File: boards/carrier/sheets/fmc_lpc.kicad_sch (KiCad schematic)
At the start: 4 parts

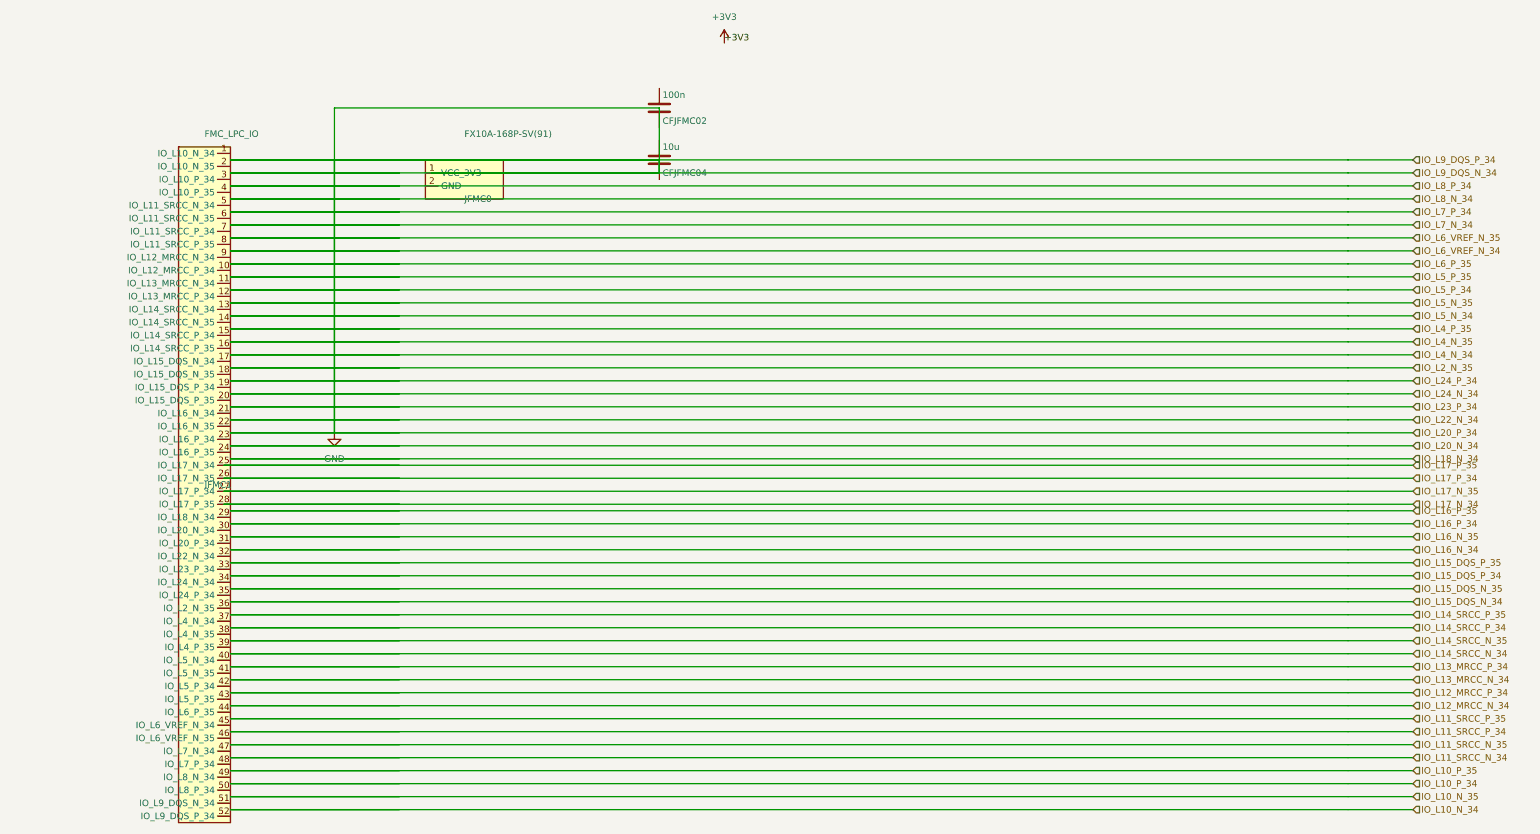
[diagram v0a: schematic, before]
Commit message: hdmi: use Connector_Generic:Conn_01x19 (Connector lib not auto-discovered)
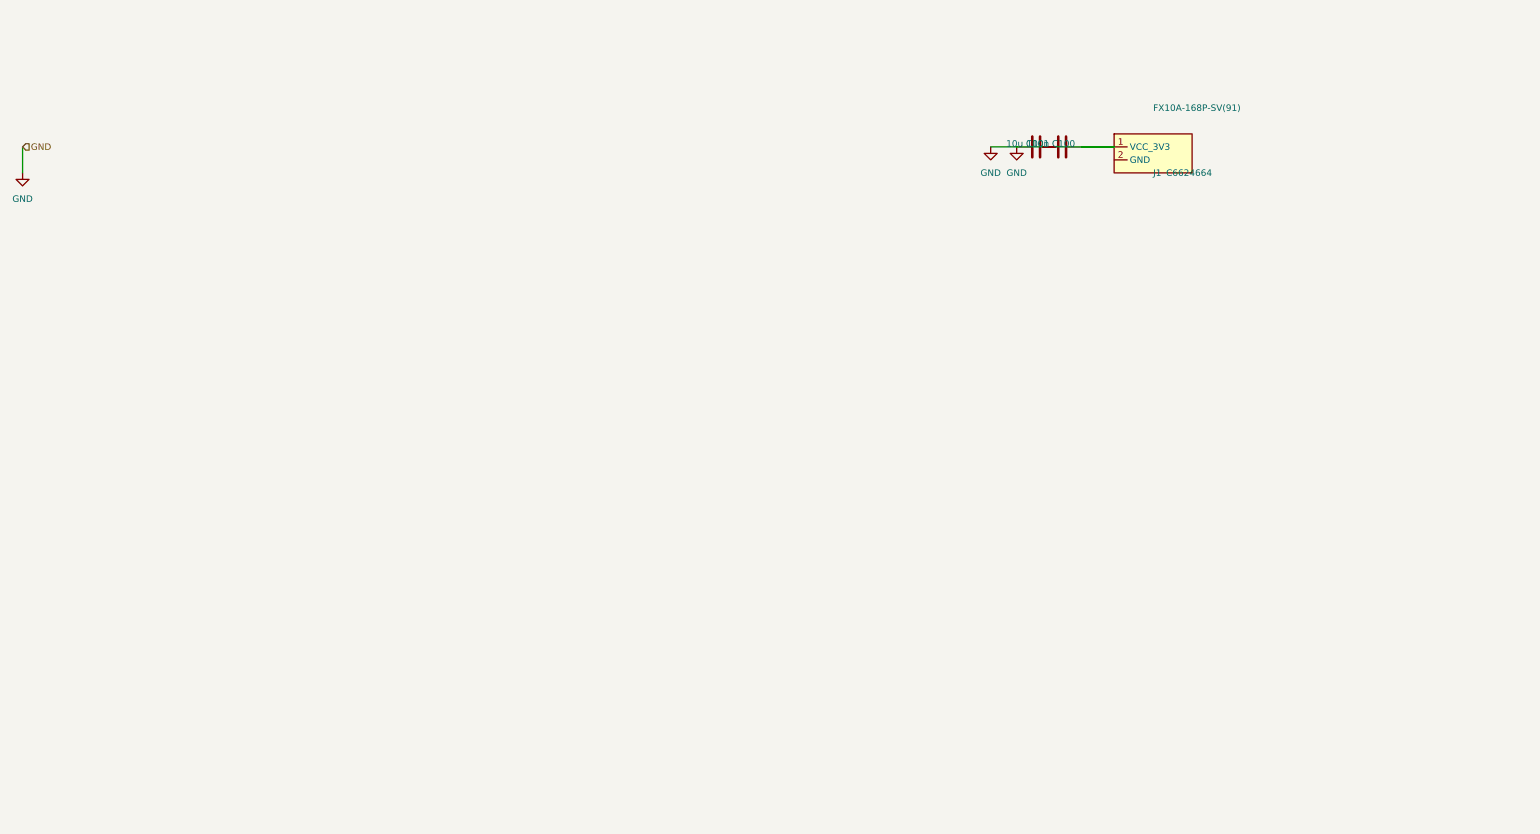
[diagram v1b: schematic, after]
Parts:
- removed CFJFMC02: 100n, Capacitor_SMD:C_0402_1005Metric, symbol Device:C
- removed CFJFMC04: 10u, Capacitor_SMD:C_0603_1608Metric, symbol Device:C
- removed JFMC0: FX10A-168P-SV(91), Connector_FFC-FPC:FX10A-168P-SV1, symbol carrier:FMC_LPC
- removed JFMC1: FMC_LPC_IO, symbol FMC_LPC_IO:FMC_LPC_IO
- added C100: 100n, Capacitor_SMD:C_0402_1005Metric, symbol Device:C
- added C101: 10u, Capacitor_SMD:C_0402_1005Metric, symbol Device:C
- added J1: FX10A-168P-SV(91), Connector_FFC-FPC:FX10A-168P-SV1, symbol zynq_eda:FMC_LPC
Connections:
- net GND: now also C100.2, C101.2
- new net: C100.1, C101.1, J1.1 (VCC_3V3)
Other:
- title: FMC LPC Connector -> FMC LPC Expansion (VITA 57.1 LPC connector)
